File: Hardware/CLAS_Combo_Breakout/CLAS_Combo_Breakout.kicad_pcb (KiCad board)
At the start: 4 copper layers, 60 x 60 mm, 88 parts, among them J1 USB_C_Receptacle_USB2.0, J2 ZED, J3 NEO, J4 USB_C_Receptacle_USB2.0, J5 Conn_SMA, U1 USBLC6-2P6, U10 NT1191GEAE3S, U2 ZED-F9P, U3 NEO-D9C-00B, U4 USBLC6-2P6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

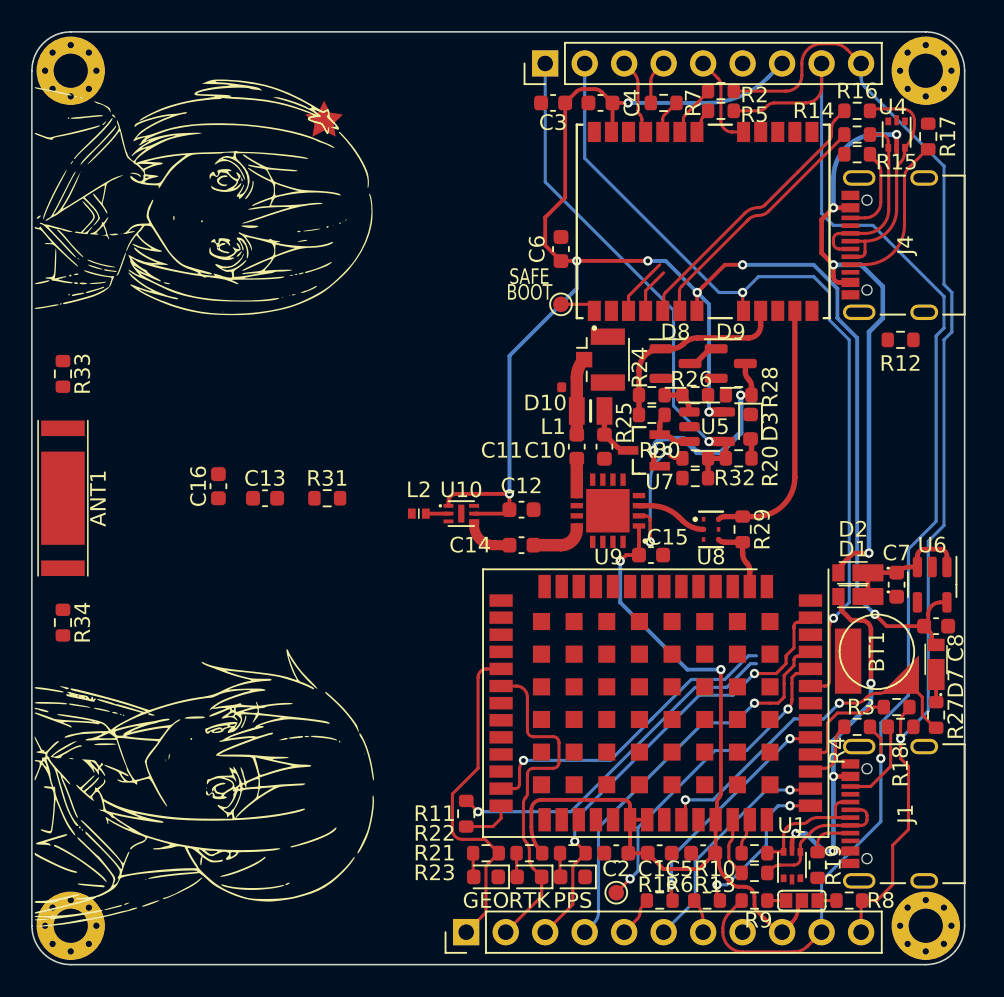
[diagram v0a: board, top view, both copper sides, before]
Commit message: GNDベタをクリアランス0.2mmで配置
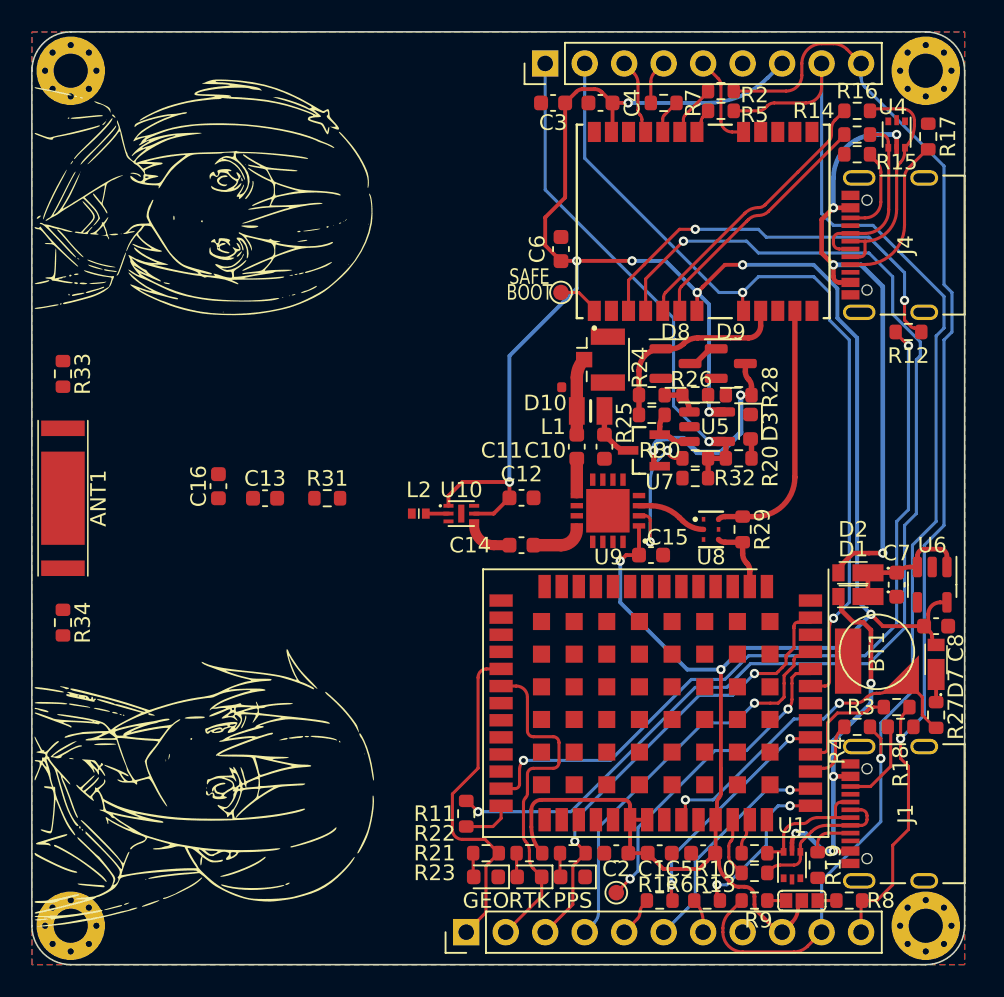
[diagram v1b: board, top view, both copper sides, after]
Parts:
- moved C12 0.76 mm to (131.5, 120.0)
- moved TP2 0.76 mm to (134.0, 106.8)
- moved R12 0.72 mm to (156.4, 109.3)
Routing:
- net Net-(R11-Pad2): track 25.8 -> 77.0 mm, vias 1 -> 2
- net Net-(R12-Pad1): track 20.7 -> 50.0 mm, vias 1 -> 2
- net Net-(R12-Pad2): track 3.79 -> 26.8 mm, vias 0 -> 2
- net +3.3V: track 169.3 -> 180.7 mm
- net /VBUS_NEO: track 39.8 -> 40.3 mm
- added copper zone on B.Cu, net GND
- added copper zone on F.Cu, net GND
- added copper zone on In1.Cu, net GND
- added copper zone on In2.Cu, net GND

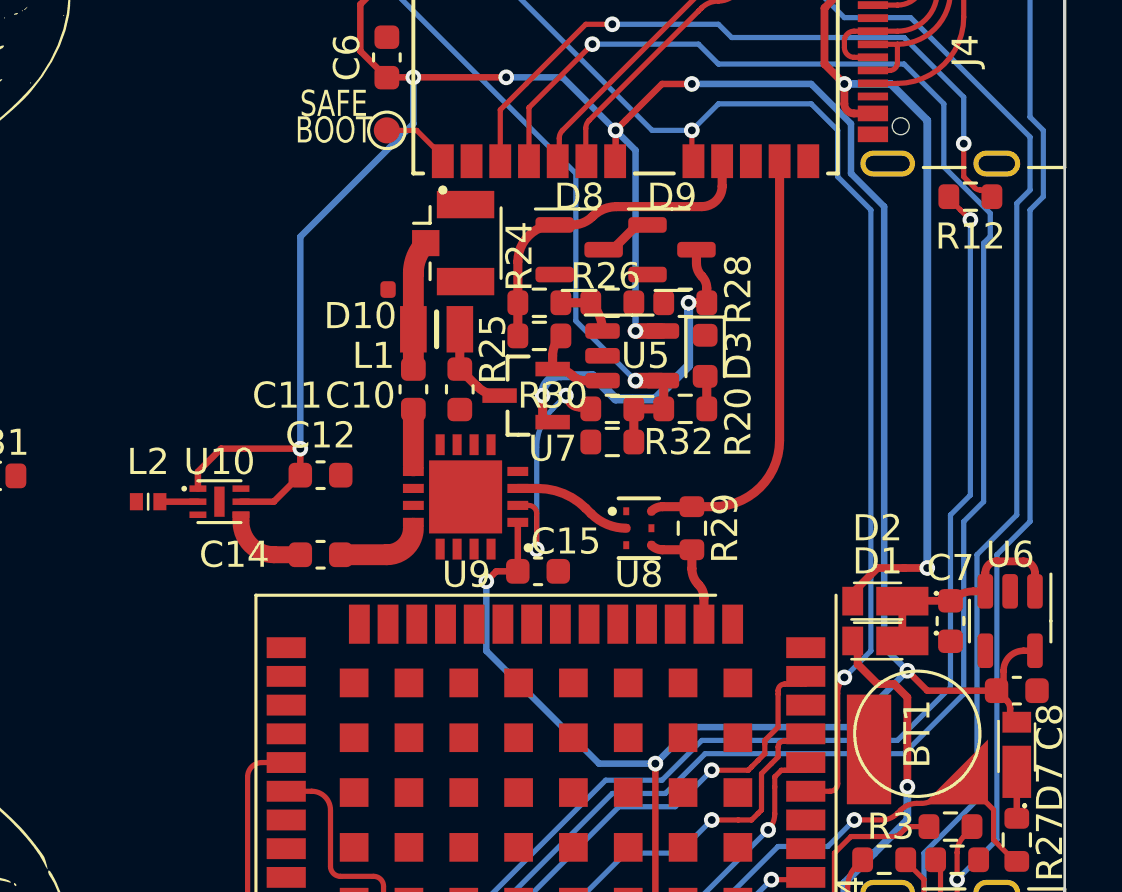
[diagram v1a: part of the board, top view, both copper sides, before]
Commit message: 伝送線路を配線中
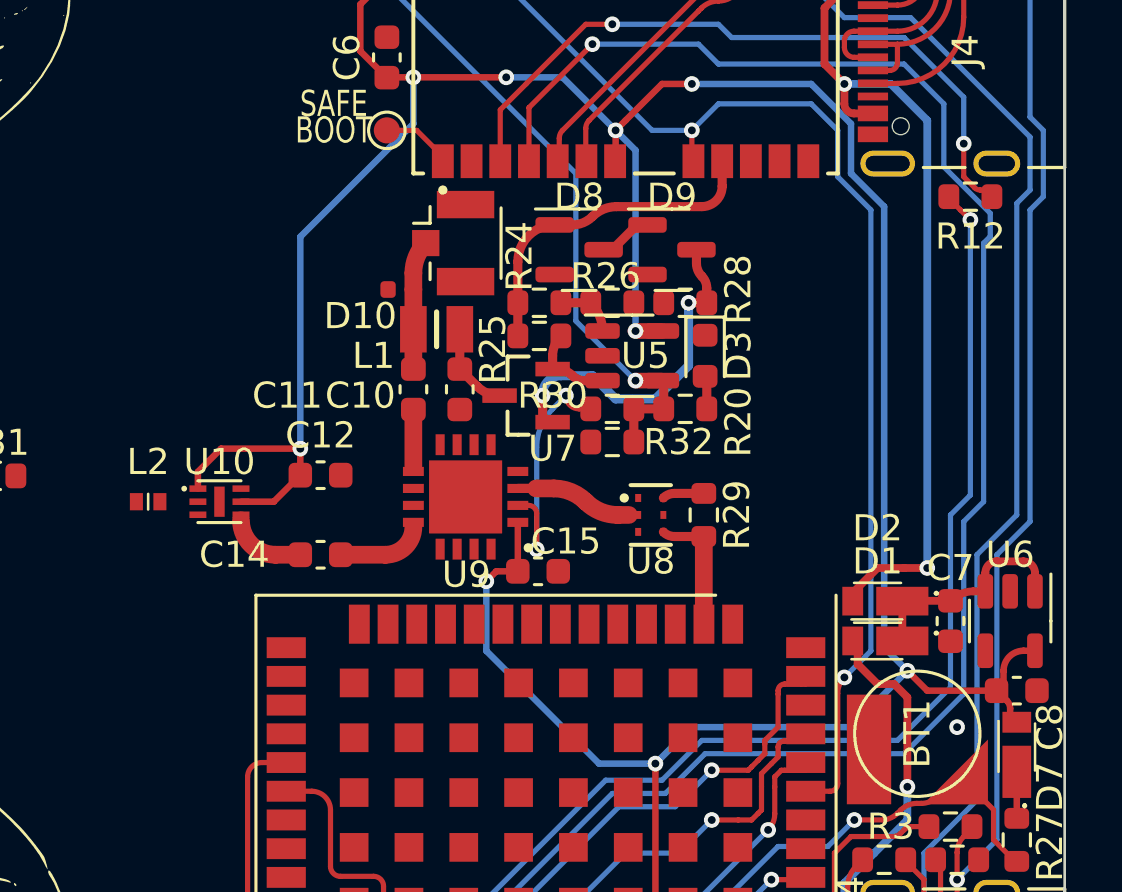
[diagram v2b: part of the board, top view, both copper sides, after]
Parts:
- moved R29 0.68 mm to (146.2, 121.5)
- moved U8 0.68 mm to (144.1, 121.5)
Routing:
- net /ANT_NEO: track 17.0 -> 1.59 mm
- net Net-(L2-Pad2): track 1.46 -> 0.00 mm
- net GND: vias 0 -> 1
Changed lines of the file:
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@@
   )
   (footprint "PD0922J5050S2HF:PD0922J5050S2HF_ANA" (layer "F.Cu")
-    (at 143.688 122.004)
+    (at 144.1452 121.496)
     (tags "PD0922J5050S2HF ")
     (property "Sheetfile" "CLAS_Combo_Breakout.kicad_sch")
@@
   )
   (footprint "Resistor_SMD:R_0603_1608Metric" (layer "F.Cu")
-    (at 145.72 122.004 90)
+    (at 146.1772 121.496 90)
     (descr "Resistor SMD 0603 (1608 Metric), square (rectangular) end terminal, IPC_7351 nominal, (Body size source: IPC-SM-782 page 72, https://www.pcb-3d.com/wordpress/wp-content/uploads/ipc-sm-782a_amendment_1_and_2.pdf), generated with kicad-footprint-generator")
     (tags "resistor")
@@
     )
   )
-  (gr_rect (start 128.123 121.738) (end 128.773 121.363) (layer "F.Cu") (width 0) (fill solid))
   (gr_line (start 100 120) (end 160 120) (layer "Dwgs.User") (width 0.1))
   (gr_line (start 100 92.5) (end 100 147.5) (layer "Edge.Cuts") (width 0.1))
@@
   (segment (start 150.927 134.196) (end 151.943 133.18) (width 0.2) (layer "B.Cu") (net 4))
   (segment (start 149.022 134.196) (end 150.927 134.196) (width 0.2) (layer "B.Cu") (net 4))
+  (via (at 155.88 129.624) (size 0.6) (drill 0.3) (layers "F.Cu" "B.Cu") (free) (net 5))
   (segment (start 135.052 104.732) (end 138.608 104.732) (width 0.25) (layer "F.Cu") (net 6))
   (segment (start 137.351 94.572) (end 136.650798 93.871798) (width 0.25) (layer "F.Cu") (net 6))
@@
   (arc (start 156.501152 124.4225) (mid 156.027523 124.516711) (end 155.626 124.785) (width 0.3) (layer "F.Cu") (net 7))
   (arc (start 158.862 123.716) (mid 158.732541 123.403459) (end 158.42 123.274) (width 0.3) (layer "F.Cu") (net 7))
-  (segment (start 135.052 117.458) (end 135.052 119.6164) (width 0.8) (layer "F.Cu") (net 8))
+  (segment (start 135.052 117.458) (end 135.052 119.6418) (width 0.678) (layer "F.Cu") (net 8))
   (segment (start 137.48679 116.56479) (end 136.83 115.908) (width 0.35) (layer "F.Cu") (net 9))
   (segment (start 136.83 115.908) (end 136.83 114.388828) (width 0.35) (layer "F.Cu") (net 9))
@@
   (arc (start 132.004 142.68321) (mid 131.937988 142.351343) (end 131.75 142.07) (width 0.2) (layer "F.Cu") (net 13))
   (arc (start 132.255377 143.819877) (mid 132.069331 143.54144) (end 132.004 143.213) (width 0.2) (layer "F.Cu") (net 13))
-  (segment (start 129.718 123.02) (end 130.721 123.02) (width 0.65) (layer "F.Cu") (net 14))
-  (arc (start 129.718 123.02) (mid 128.819974 122.648026) (end 128.448 121.75) (width 0.65) (layer "F.Cu") (net 14))
-  (segment (start 135.052 115.908) (end 135.052 114.384) (width 0.8) (layer "F.Cu") (net 15))
-  (segment (start 135.052 114.384) (end 135.052 112.226337) (width 0.8) (layer "F.Cu") (net 15))
-  (arc (start 135.052 112.226337) (mid 135.175188 111.607027) (end 135.526 111.082) (width 0.8) (layer "F.Cu") (net 15))
-  (segment (start 132.271 123.02) (end 134.036 123.02) (width 0.8) (layer "F.Cu") (net 17))
-  (arc (start 134.036 123.02) (mid 134.75442 122.72242) (end 135.052 122.004) (width 0.8) (layer "F.Cu") (net 17))
+  (segment (start 130.721 123.02) (end 129.7688 123.02) (width 0.678) (layer "F.Cu") (net 14))
+  (arc (start 129.7688 123.02) (mid 128.834853 122.633147) (end 128.448 121.6992) (width 0.678) (layer "F.Cu") (net 14))
+  (segment (start 135.052 112.86) (end 135.052 112.226337) (width 0.678) (layer "F.Cu") (net 15))
+  (segment (start 135.052 115.908) (end 135.052 112.86) (width 0.678) (layer "F.Cu") (net 15))
+  (arc (start 135.052 112.226337) (mid 135.175188 111.607027) (end 135.526 111.082) (width 0.678) (layer "F.Cu") (net 15))
+  (segment (start 132.271 123.02) (end 133.9852 123.02) (width 0.678) (layer "F.Cu") (net 17))
+  (arc (start 133.9852 123.02) (mid 134.739542 122.707542) (end 135.052 121.9532) (width 0.678) (layer "F.Cu") (net 17))
   (segment (start 150.533867 140.542) (end 152.655 140.542) (width 0.2) (layer "F.Cu") (net 18))
   (segment (start 152.655 139.542) (end 152.058 139.542) (width 0.2) (layer "F.Cu") (net 18))
@@
   (segment (start 147.307 145.88) (end 148.514 145.88) (width 0.2) (layer "F.Cu") (net 24))
   (segment (start 150.546 145.88) (end 151.753 145.88) (width 0.2) (layer "F.Cu") (net 25))
-  (segment (start 126.798 120.988) (end 125.342 120.988) (width 0.25) (layer "F.Cu") (net 27))
   (segment (start 154.356 145.88) (end 153.403 145.88) (width 0.2) (layer "F.Cu") (net 28))
   (segment (start 149.53 92.794) (end 149.53 92.032) (width 0.2) (layer "F.Cu") (net 28))
@@
   (segment (start 136.179999 107.764999) (end 136.179999 107.9451) (width 0.2) (layer "F.Cu") (net 44))
   (segment (start 134.036 106.764) (end 135.179 106.764) (width 0.2) (layer "F.Cu") (net 44))
-  (segment (start 146.182 125.68) (end 146.182 124.665156) (width 0.35) (layer "F.Cu") (net 47))
-  (segment (start 145.72 123.54979) (end 145.72 122.829) (width 0.35) (layer "F.Cu") (net 47))
-  (segment (start 145.72 122.829) (end 144.593089 122.829) (width 0.35) (layer "F.Cu") (net 47))
-  (arc (start 144.593089 122.829) (mid 144.364439 122.783519) (end 144.1706 122.653999) (width 0.35) (layer "F.Cu") (net 47))
-  (arc (start 145.974 124.163) (mid 145.786012 123.881657) (end 145.72 123.54979) (width 0.35) (layer "F.Cu") (net 47))
-  (arc (start 146.182 124.665156) (mid 146.127943 124.393391) (end 145.974 124.163) (width 0.35) (layer "F.Cu") (net 47))
+  (segment (start 146.1772 122.321) (end 146.1772 125.668412) (width 0.678) (layer "F.Cu") (net 47))
+  (segment (start 146.1772 122.321) (end 145.050289 122.321) (width 0.35) (layer "F.Cu") (net 47))
+  (arc (start 146.1772 125.668412) (mid 146.178448 125.674683) (end 146.182 125.68) (width 0.678) (layer "F.Cu") (net 47))
+  (arc (start 145.050289 122.321) (mid 144.821639 122.275519) (end 144.6278 122.145999) (width 0.35) (layer "F.Cu") (net 47))
   (segment (start 148.768 138.768) (end 149.86955 138.768) (width 0.2) (layer "F.Cu") (net 71))
   (via (at 148.768 138.768) (size 0.6) (drill 0.3) (layers "F.Cu" "B.Cu") (free) (net 71))
@@
   (segment (start 135.56 147.912) (end 136.179592 147.292408) (width 0.2) (layer "B.Cu") (net 74))
   (arc (start 136.179592 147.292408) (mid 136.378983 146.993998) (end 136.449 146.642) (width 0.2) (layer "B.Cu") (net 74))
-  (segment (start 149.08 107.9451) (end 149.08 118.644) (width 0.35) (layer "F.Cu") (net 78))
-  (segment (start 146.545 121.179) (end 145.72 121.179) (width 0.35) (layer "F.Cu") (net 78))
-  (segment (start 145.72 121.179) (end 144.593089 121.179) (width 0.35) (layer "F.Cu") (net 78))
-  (arc (start 144.593089 121.179) (mid 144.36444 121.224481) (end 144.1706 121.354001) (width 0.35) (layer "F.Cu") (net 78))
-  (arc (start 149.08 118.644) (mid 148.337516 120.436516) (end 146.545 121.179) (width 0.35) (layer "F.Cu") (net 78))
+  (segment (start 146.1772 120.671) (end 145.050289 120.671) (width 0.35) (layer "F.Cu") (net 78))
+  (arc (start 145.050289 120.671) (mid 144.82164 120.716481) (end 144.6278 120.846001) (width 0.35) (layer "F.Cu") (net 78))
   (segment (start 144.323 93.429) (end 144.323 95.715) (width 0.2) (layer "F.Cu") (net 82))
   (segment (start 145.0469 96.4389) (end 145.779999 96.4389) (width 0.2) (layer "F.Cu") (net 82))
@@
   (segment (start 127.94 141.117) (end 129.655 141.117) (width 0.2) (layer "F.Cu") (net 102))
   (segment (start 129.655 141.117) (end 130.182 140.59) (width 0.2) (layer "F.Cu") (net 102))
-  (segment (start 141.656 121.242) (end 141.861224 121.447224) (width 0.35) (layer "F.Cu") (net 103))
-  (segment (start 139.052 120.48) (end 139.81637 120.48) (width 0.35) (layer "F.Cu") (net 103))
-  (arc (start 141.861224 121.447224) (mid 142.477937 121.859299) (end 143.2054 122.004) (width 0.35) (layer "F.Cu") (net 103))
-  (arc (start 139.81637 120.48) (mid 140.81197 120.678038) (end 141.656 121.242) (width 0.35) (layer "F.Cu") (net 103))
+  (segment (start 139.052 120.48) (end 139.751 120.48) (width 0.35) (layer "F.Cu") (net 103))
+  (segment (start 139.751 120.48) (end 140.42958 120.48) (width 0.678) (layer "F.Cu") (net 103))
+  (segment (start 142.88242 121.496) (end 143.307 121.496) (width 0.678) (layer "F.Cu") (net 103))
+  (arc (start 140.42958 120.48) (mid 141.093313 120.612025) (end 141.656 120.988) (width 0.678) (layer "F.Cu") (net 103))
+  (arc (start 141.656 120.988) (mid 142.218686 121.363975) (end 142.88242 121.496) (width 0.678) (layer "F.Cu") (net 103))
   (segment (start 128.004 139.467) (end 128.702 140.165) (width 0.2) (layer "F.Cu") (net 105))
   (segment (start 139.48 107.9451) (end 139.48 105.892) (width 0.2) (layer "F.Cu") (net 105))

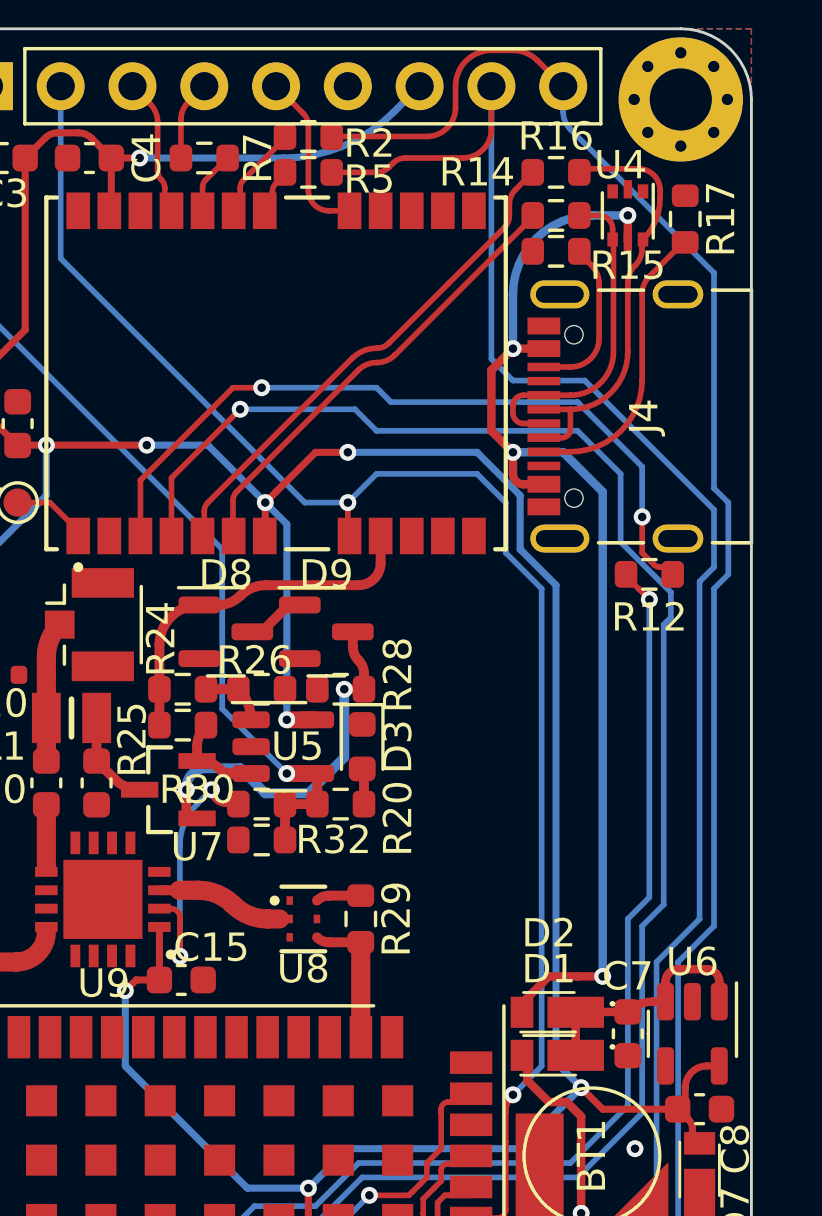
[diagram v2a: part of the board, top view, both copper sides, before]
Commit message: 伝送線路を配線
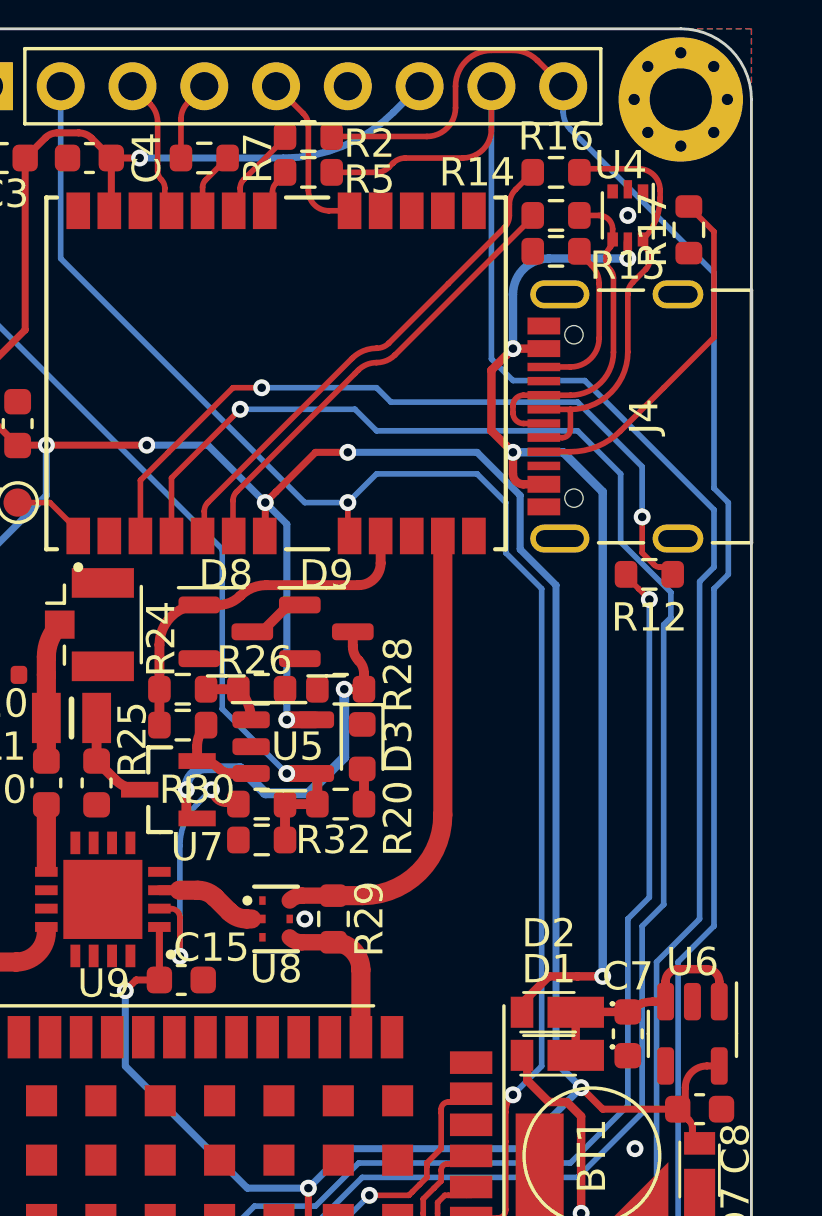
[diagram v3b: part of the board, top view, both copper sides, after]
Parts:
- moved R29 0.97 mm to (145.2, 121.5)
- moved U8 0.97 mm to (143.2, 121.5)
- moved R17 0.40 mm to (157.8, 97.1), turned to -90 degrees
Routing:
- net /ANT_NEO: track 1.59 -> 16.8 mm
- net /CC1_NEO: track 10.3 -> 12.6 mm
- net /VBUS_NEO: track 40.3 -> 39.2 mm
- net Net-(U8-Pad2): track 4.51 -> 3.60 mm
- net /ANT_ZED: track 4.95 -> 5.47 mm
- net GND: vias 1 -> 3
